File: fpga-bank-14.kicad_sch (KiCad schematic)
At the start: 1 part

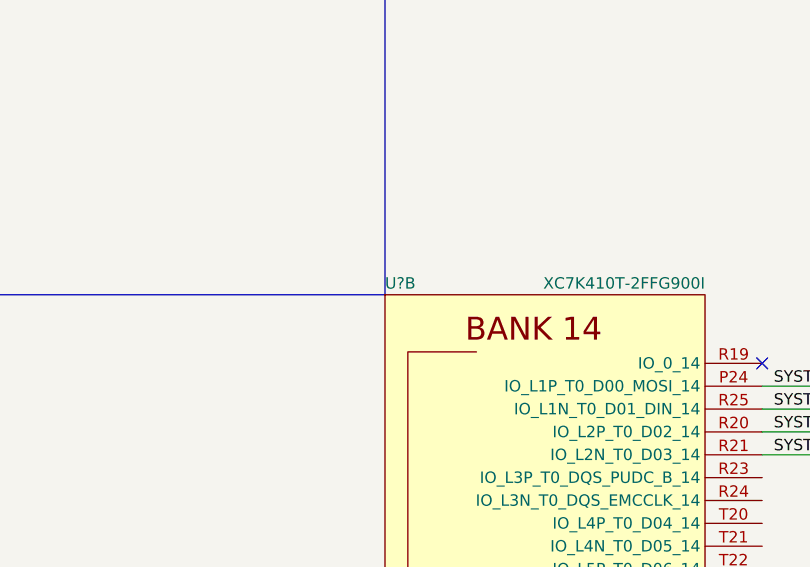
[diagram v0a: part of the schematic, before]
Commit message: Fix FPGA symbol
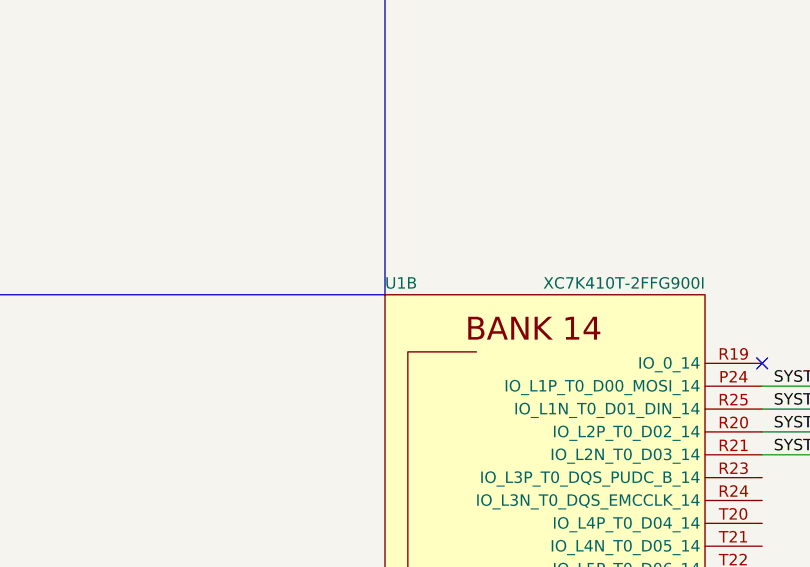
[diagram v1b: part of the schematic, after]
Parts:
- gave numbers to parts that had none: 1
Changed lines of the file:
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@@
     (effects (font (size 1.27 1.27)) (justify left))
   )
-  (symbol (lib_name "XC7K410T-2FFG900I_1") (lib_id "antmicroMicrocontrollers:XC7K410T-2FFG900I") (at 119.38 144.78 0) (unit 2)
+  (symbol (lib_id "antmicroMicrocontrollers:XC7K410T-2FFG900I") (at 119.38 144.78 0) (unit 2)
     (in_bom yes) (on_board yes)
-    (property "Reference" "U?" (id 0) (at 101.6 74.93 0)
+    (property "Reference" "U1" (id 0) (at 101.6 74.93 0)
       (effects (font (size 1.27 1.27)) (justify left))
     )

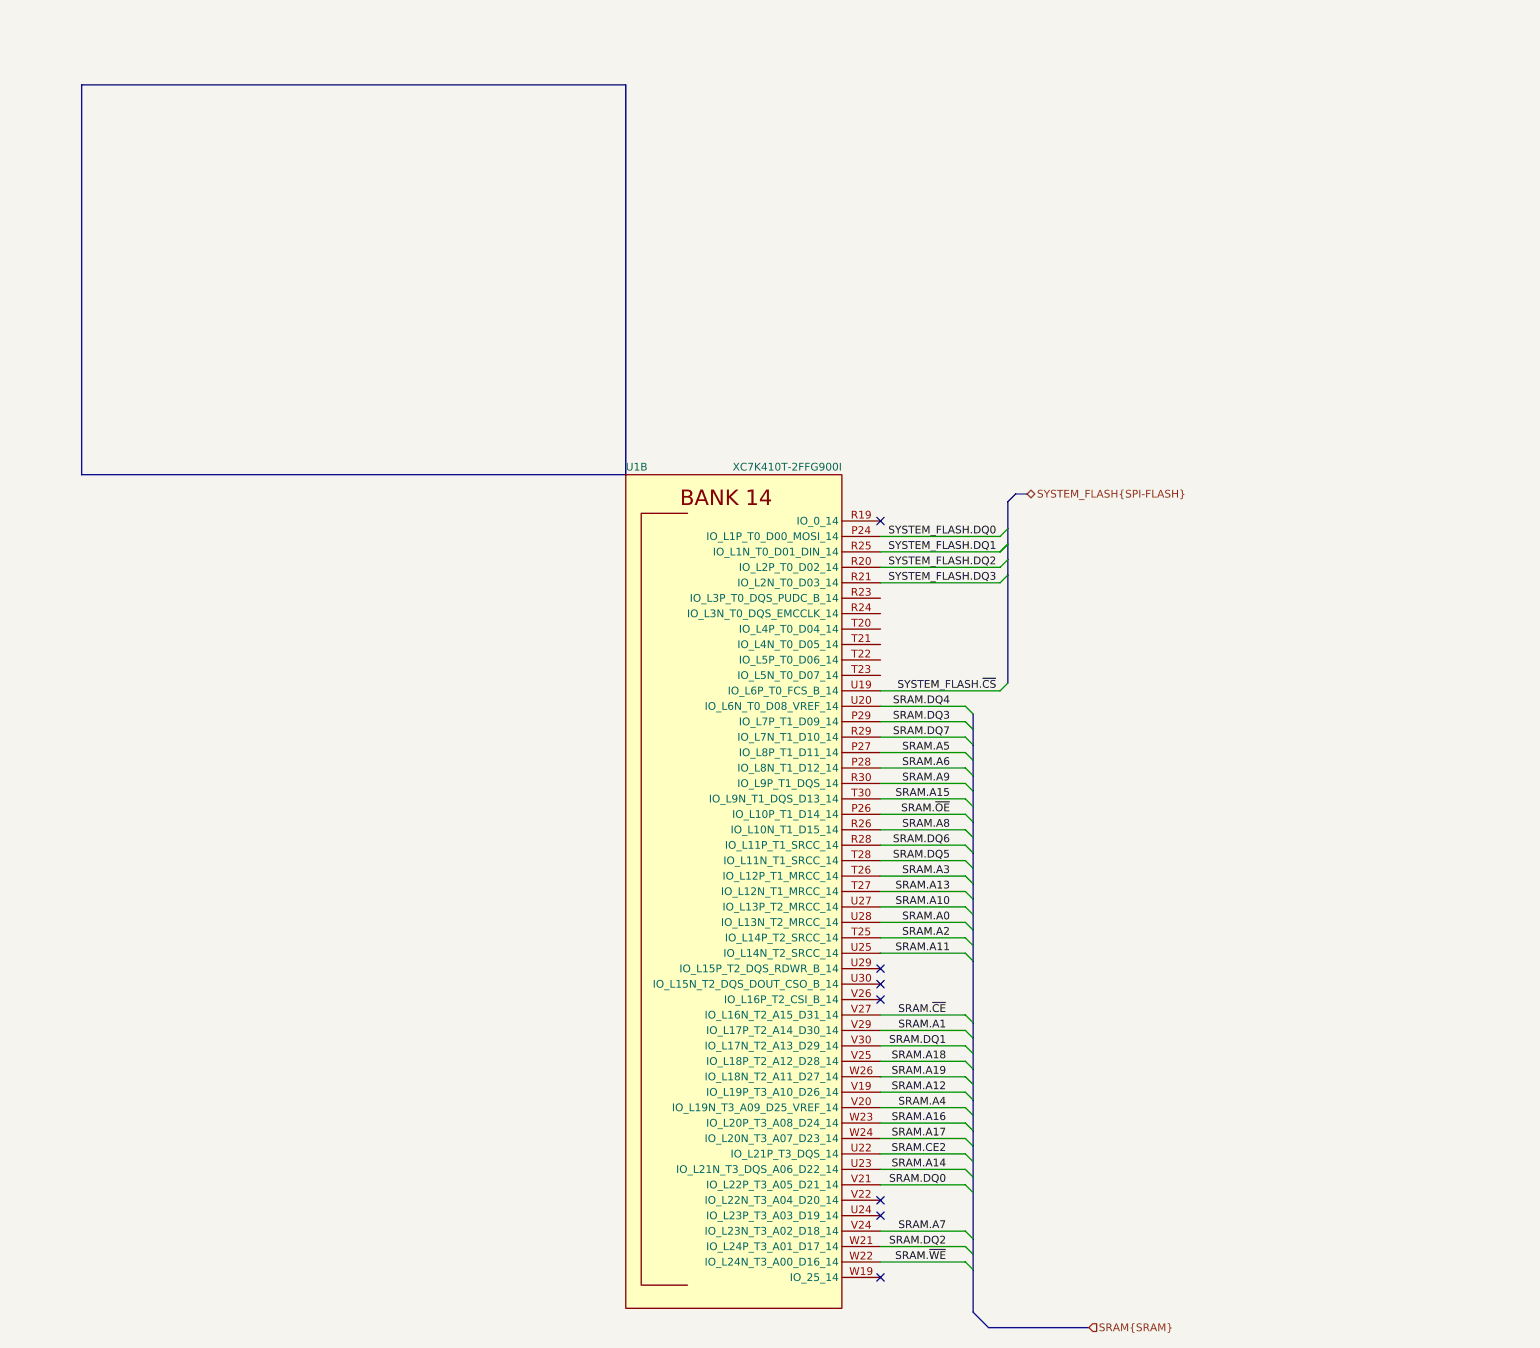
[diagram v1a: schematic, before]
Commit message: Connect SPI bus
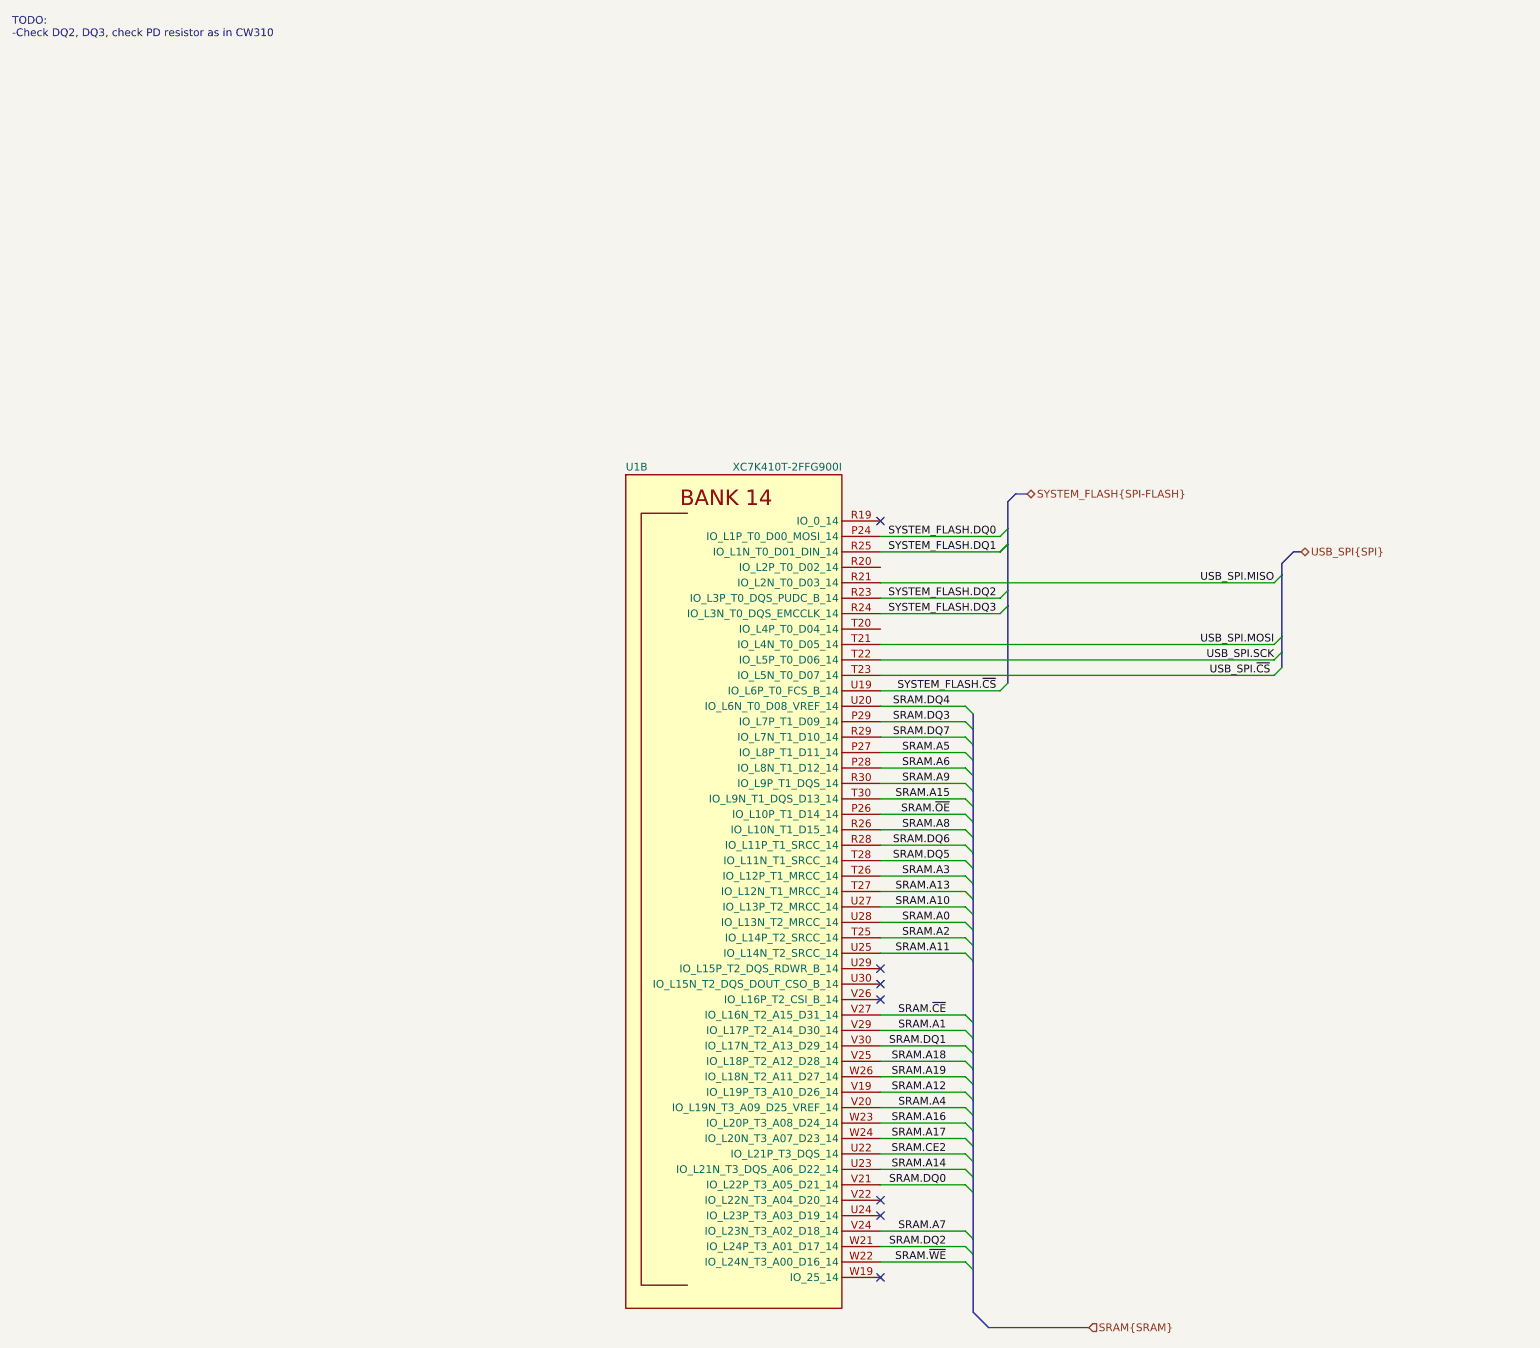
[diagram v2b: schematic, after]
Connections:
- net SYSTEM_FLASH.DQ2: now also U1.R23 (IO_L3P_T0_DQS_PUDC_B_14); no longer U1.R20 (IO_L2P_T0_D02_14)
- net SYSTEM_FLASH.DQ3: now also U1.R24 (IO_L3N_T0_DQS_EMCCLK_14); no longer U1.R21 (IO_L2N_T0_D03_14)
- net USB_SPI.MOSI: now reaches U1.T21 (IO_L4N_T0_D05_14)
- net USB_SPI.SCK: now reaches U1.T22 (IO_L5P_T0_D06_14)
- net USB_SPI.~{CS}: now reaches U1.T23 (IO_L5N_T0_D07_14)
- new net USB_SPI.MISO: U1.R21 (IO_L2N_T0_D03_14)
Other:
- note added: "TODO: -Check DQ2, DQ3, check PD resistor as in CW310"
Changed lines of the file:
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@@
     (stroke (width 0) (type default) (color 0 0 0 0))
   )
-  (bus_entry (at 164.465 90.17) (size -1.27 1.27)
+  (bus_entry (at 164.465 95.25) (size -1.27 1.27)
     (stroke (width 0) (type default) (color 0 0 0 0))
   )
@@
     (stroke (width 0) (type default) (color 0 0 0 0))
   )
+  (bus_entry (at 209.55 92.71) (size -1.27 1.27)
+    (stroke (width 0) (type default) (color 0 0 0 0))
+  )
+  (bus_entry (at 209.55 102.87) (size -1.27 1.27)
+    (stroke (width 0) (type default) (color 0 0 0 0))
+  )
   (bus_entry (at 157.48 205.74) (size 1.27 1.27)
     (stroke (width 0) (type default) (color 0 0 0 0))
@@
     (stroke (width 0) (type default) (color 0 0 0 0))
   )
+  (bus_entry (at 209.55 105.41) (size -1.27 1.27)
+    (stroke (width 0) (type default) (color 0 0 0 0))
+  )
   (bus_entry (at 157.48 144.78) (size 1.27 1.27)
     (stroke (width 0) (type default) (color 0 0 0 0))
@@
     (stroke (width 0) (type default) (color 0 0 0 0))
   )
+  (bus_entry (at 209.55 107.95) (size -1.27 1.27)
+    (stroke (width 0) (type default) (color 0 0 0 0))
+  )
   (bus_entry (at 157.48 180.34) (size 1.27 1.27)
     (stroke (width 0) (type default) (color 0 0 0 0))
@@
     (stroke (width 0) (type default) (color 0 0 0 0))
   )
-  (bus_entry (at 164.465 92.71) (size -1.27 1.27)
+  (bus_entry (at 164.465 97.79) (size -1.27 1.27)
     (stroke (width 0) (type default) (color 0 0 0 0))
   )
@@
     (stroke (width 0) (type default) (color 0 0 0 0))
   )
-  (polyline (pts (xy 101.6 12.065) (xy 101.6 76.2))
-    (stroke (width 0) (type default) (color 0 0 0 0))
-  )
   (wire (pts (xy 157.48 121.92) (xy 143.51 121.92))
     (stroke (width 0) (type default) (color 0 0 0 0))
@@
     (stroke (width 0) (type default) (color 0 0 0 0))
   )
+  (bus (pts (xy 209.55 90.805) (xy 209.55 92.71))
+    (stroke (width 0) (type default) (color 0 0 0 0))
+  )
   (wire (pts (xy 163.195 111.76) (xy 143.51 111.76))
     (stroke (width 0) (type default) (color 0 0 0 0))
@@
     (stroke (width 0) (type default) (color 0 0 0 0))
   )
-  (bus (pts (xy 164.465 92.71) (xy 164.465 110.49))
-    (stroke (width 0) (type default) (color 0 0 0 0))
-  )
   (bus (pts (xy 158.75 201.93) (xy 158.75 204.47))
     (stroke (width 0) (type default) (color 0 0 0 0))
@@
     (stroke (width 0) (type default) (color 0 0 0 0))
   )
+  (bus (pts (xy 211.455 88.9) (xy 212.725 88.9))
+    (stroke (width 0) (type default) (color 0 0 0 0))
+  )
   (bus (pts (xy 158.75 179.07) (xy 158.75 181.61))
     (stroke (width 0) (type default) (color 0 0 0 0))
@@
     (stroke (width 0) (type default) (color 0 0 0 0))
   )
-  (bus (pts (xy 164.465 90.17) (xy 164.465 92.71))
-    (stroke (width 0) (type default) (color 0 0 0 0))
-  )
   (bus (pts (xy 158.75 184.15) (xy 158.75 186.69))
     (stroke (width 0) (type default) (color 0 0 0 0))
@@
     (stroke (width 0) (type default) (color 0 0 0 0))
   )
-  (polyline (pts (xy 101.6 12.065) (xy 12.065 12.065))
-    (stroke (width 0) (type default) (color 0 0 0 0))
-  )
   (bus (pts (xy 165.735 79.375) (xy 167.64 79.375))
     (stroke (width 0) (type default) (color 0 0 0 0))
   )
+  (bus (pts (xy 209.55 92.71) (xy 209.55 102.87))
+    (stroke (width 0) (type default) (color 0 0 0 0))
+  )
   (bus (pts (xy 158.75 151.13) (xy 158.75 153.67))
     (stroke (width 0) (type default) (color 0 0 0 0))
@@
     (stroke (width 0) (type default) (color 0 0 0 0))
   )
-  (polyline (pts (xy 12.065 76.2) (xy 101.6 76.2))
-    (stroke (width 0) (type default) (color 0 0 0 0))
-  )
   (bus (pts (xy 164.465 80.645) (xy 164.465 85.09))
     (stroke (width 0) (type default) (color 0 0 0 0))
@@
     (stroke (width 0) (type default) (color 0 0 0 0))
   )
-  (bus (pts (xy 164.465 87.63) (xy 164.465 90.17))
+  (bus (pts (xy 164.465 87.63) (xy 164.465 95.25))
     (stroke (width 0) (type default) (color 0 0 0 0))
   )
@@
     (stroke (width 0) (type default) (color 0 0 0 0))
   )
-  (wire (pts (xy 163.195 93.98) (xy 143.51 93.98))
+  (bus (pts (xy 209.55 90.805) (xy 211.455 88.9))
+    (stroke (width 0) (type default) (color 0 0 0 0))
+  )
+  (bus (pts (xy 164.465 97.79) (xy 164.465 110.49))
+    (stroke (width 0) (type default) (color 0 0 0 0))
+  )
+  (wire (pts (xy 163.195 99.06) (xy 143.51 99.06))
     (stroke (width 0) (type default) (color 0 0 0 0))
   )
@@
     (stroke (width 0) (type default) (color 0 0 0 0))
   )
+  (wire (pts (xy 143.51 104.14) (xy 208.28 104.14))
+    (stroke (width 0) (type default) (color 0 0 0 0))
+  )
   (bus (pts (xy 158.75 168.91) (xy 158.75 171.45))
     (stroke (width 0) (type default) (color 0 0 0 0))
   )
-  (wire (pts (xy 163.195 91.44) (xy 143.51 91.44))
+  (wire (pts (xy 163.195 96.52) (xy 143.51 96.52))
+    (stroke (width 0) (type default) (color 0 0 0 0))
+  )
+  (bus (pts (xy 164.465 95.25) (xy 164.465 97.79))
     (stroke (width 0) (type default) (color 0 0 0 0))
   )
@@
     (stroke (width 0) (type default) (color 0 0 0 0))
   )
+  (wire (pts (xy 143.51 106.68) (xy 208.28 106.68))
+    (stroke (width 0) (type default) (color 0 0 0 0))
+  )
   (bus (pts (xy 164.465 80.645) (xy 165.735 79.375))
     (stroke (width 0) (type default) (color 0 0 0 0))
@@
     (stroke (width 0) (type default) (color 0 0 0 0))
   )
+  (wire (pts (xy 143.51 109.22) (xy 208.28 109.22))
+    (stroke (width 0) (type default) (color 0 0 0 0))
+  )
   (wire (pts (xy 157.48 119.38) (xy 143.51 119.38))
     (stroke (width 0) (type default) (color 0 0 0 0))
@@
     (stroke (width 0) (type default) (color 0 0 0 0))
   )
+  (bus (pts (xy 209.55 102.87) (xy 209.55 105.41))
+    (stroke (width 0) (type default) (color 0 0 0 0))
+  )
   (bus (pts (xy 158.75 115.57) (xy 158.75 118.11))
     (stroke (width 0) (type default) (color 0 0 0 0))
@@
     (stroke (width 0) (type default) (color 0 0 0 0))
   )
-  (polyline (pts (xy 12.065 12.065) (xy 12.065 76.2))
-    (stroke (width 0) (type default) (color 0 0 0 0))
-  )
   (wire (pts (xy 157.48 180.34) (xy 143.51 180.34))
     (stroke (width 0) (type default) (color 0 0 0 0))
@@
     (stroke (width 0) (type default) (color 0 0 0 0))
   )
+  (bus (pts (xy 209.55 105.41) (xy 209.55 107.95))
+    (stroke (width 0) (type default) (color 0 0 0 0))
+  )
   (wire (pts (xy 157.48 137.16) (xy 143.51 137.16))
     (stroke (width 0) (type default) (color 0 0 0 0))
@@
     (stroke (width 0) (type default) (color 0 0 0 0))
   )
+  (wire (pts (xy 143.51 93.98) (xy 208.28 93.98))
+    (stroke (width 0) (type default) (color 0 0 0 0))
+  )
   (wire (pts (xy 157.48 177.8) (xy 143.51 177.8))
     (stroke (width 0) (type default) (color 0 0 0 0))
   )
+  (text "TODO:\n-Check DQ2, DQ3, check PD resistor as in CW310\n"
+    (at 0.635 4.445 0)
+    (effects (font (size 1.27 1.27)) (justify left bottom))
+  )
   (label "SRAM.DQ4" (at 154.94 114.3 180)
     (effects (font (size 1.27 1.27)) (justify right bottom))
@@
     (effects (font (size 1.27 1.27)) (justify right bottom))
   )
+  (label "USB_SPI.~{CS}" (at 207.645 109.22 180)
+    (effects (font (size 1.27 1.27)) (justify right bottom))
+  )
   (label "SRAM.DQ6" (at 154.94 137.16 180)
     (effects (font (size 1.27 1.27)) (justify right bottom))
@@
     (effects (font (size 1.27 1.27)) (justify right bottom))
   )
+  (label "USB_SPI.MOSI" (at 208.28 104.14 180)
+    (effects (font (size 1.27 1.27)) (justify right bottom))
+  )
+  (label "USB_SPI.SCK" (at 208.28 106.68 180)
+    (effects (font (size 1.27 1.27)) (justify right bottom))
+  )
   (label "SRAM.A1" (at 154.305 167.64 180)
     (effects (font (size 1.27 1.27)) (justify right bottom))
@@
     (effects (font (size 1.27 1.27)) (justify right bottom))
   )
-  (label "SYSTEM_FLASH.DQ3" (at 162.56 93.98 180)
+  (label "SYSTEM_FLASH.DQ3" (at 162.56 99.06 180)
     (effects (font (size 1.27 1.27)) (justify right bottom))
   )
@@
     (effects (font (size 1.27 1.27)) (justify right bottom))
   )
-  (label "SYSTEM_FLASH.DQ2" (at 162.56 91.44 180)
+  (label "USB_SPI.MISO" (at 208.28 93.98 180)
+    (effects (font (size 1.27 1.27)) (justify right bottom))
+  )
+  (label "SYSTEM_FLASH.DQ2" (at 162.56 96.52 180)
     (effects (font (size 1.27 1.27)) (justify right bottom))
   )
@@
     (effects (font (size 1.27 1.27)) (justify left))
   )
+  (hierarchical_label "USB_SPI{SPI}" (shape bidirectional) (at 212.725 88.9 0)
+    (effects (font (size 1.27 1.27)) (justify left))
+  )
